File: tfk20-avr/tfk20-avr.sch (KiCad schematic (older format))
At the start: 31 parts, among them J1 USB_C_Receptacle_USB2.0, J2 AVR-ISP-6, SW1 Reset, U1 ATmega32U4-AU, Y1 16MHz

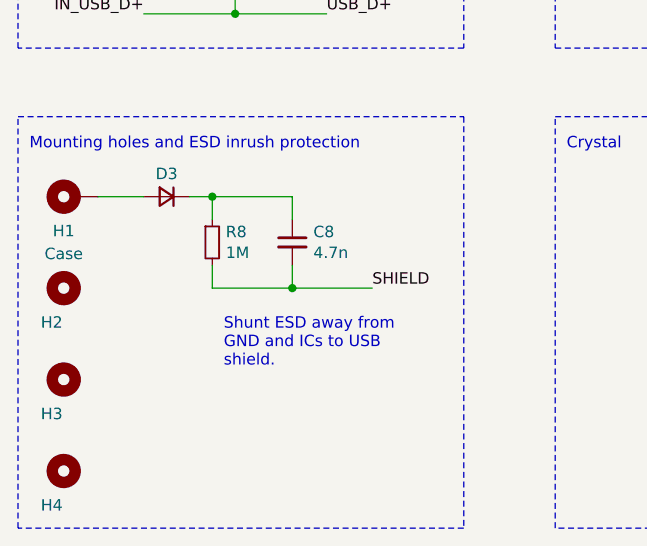
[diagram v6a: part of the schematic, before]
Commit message: Finish north-facing LED footprint layout
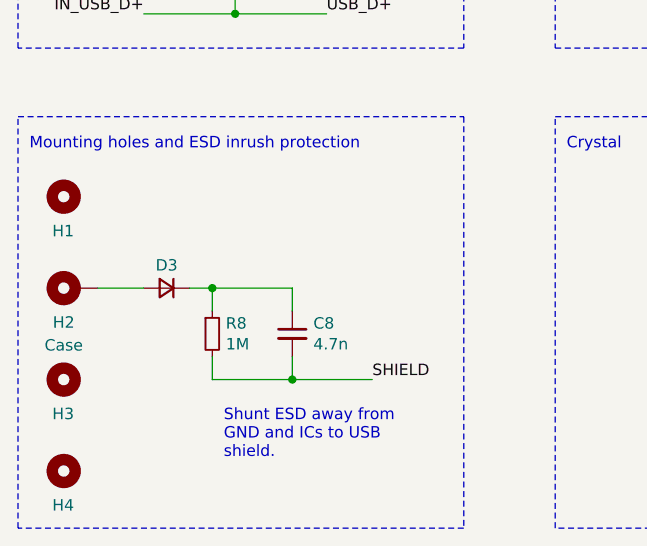
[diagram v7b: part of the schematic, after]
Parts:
- renumbered H2 to H1, H1 to H2
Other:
- moved on the sheet: C8, D3, H1, H2, R8
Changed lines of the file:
@@
 L Device:D_Small D3
 U 1 1 60989164
-P 1350 6150
+P 1350 6550
 AR Path="/60989164" Ref="D3"  Part="1"
 AR Path="/60815FFC/60989164" Ref="D?"  Part="1"
-F 0 "D3" H 1350 6050 50  0000 C CNN
-F 1 "Case ESD" H 1350 6034 50  0001 C CNN
-F 2 "Diode_SMD:D_SOD-123" V 1350 6150 50  0001 C CNN
-F 3 "~" V 1350 6150 50  0001 C CNN
-	1    1350 6150
+F 0 "D3" H 1350 6450 50  0000 C CNN
+F 1 "Case ESD" H 1350 6434 50  0001 C CNN
+F 2 "Diode_SMD:D_SOD-123" V 1350 6550 50  0001 C CNN
+F 3 "~" V 1350 6550 50  0001 C CNN
+	1    1350 6550
 	-1   0    0    1
 $EndComp
 Wire Wire Line
-	1450 6150 1550 6150
-Wire Wire Line
-	1550 6150 1550 6250
-Wire Wire Line
-	1550 6150 1900 6150
-Wire Wire Line
-	1900 6150 1900 6250
-Connection ~ 1550 6150
+	1450 6550 1550 6550
+Wire Wire Line
+	1550 6550 1550 6650
+Wire Wire Line
+	1550 6550 1900 6550
+Wire Wire Line
+	1900 6550 1900 6650
+Connection ~ 1550 6550
 $Comp
 L Device:R_Small R8
 U 1 1 6098916F
-P 1550 6350
+P 1550 6750
 AR Path="/6098916F" Ref="R8"  Part="1"
 AR Path="/60815FFC/6098916F" Ref="R?"  Part="1"
-F 0 "R8" H 1609 6396 50  0000 L CNN
-F 1 "1M" H 1609 6305 50  0000 L CNN
-F 2 "Resistor_SMD:R_0805_2012Metric_Pad1.20x1.40mm_HandSolder" H 1550 6350 50  0001 C CNN
-F 3 "~" H 1550 6350 50  0001 C CNN
-	1    1550 6350
+F 0 "R8" H 1609 6796 50  0000 L CNN
+F 1 "1M" H 1609 6705 50  0000 L CNN
+F 2 "Resistor_SMD:R_0805_2012Metric_Pad1.20x1.40mm_HandSolder" H 1550 6750 50  0001 C CNN
+F 3 "~" H 1550 6750 50  0001 C CNN
+	1    1550 6750
 	1    0    0    -1
 $EndComp
@@
 L Device:C_Small C8
 U 1 1 60989175
-P 1900 6350
+P 1900 6750
 AR Path="/60989175" Ref="C8"  Part="1"
 AR Path="/60815FFC/60989175" Ref="C?"  Part="1"
-F 0 "C8" H 1992 6396 50  0000 L CNN
-F 1 "4.7n" H 1992 6305 50  0000 L CNN
-F 2 "Capacitor_SMD:C_0805_2012Metric_Pad1.18x1.45mm_HandSolder" H 1900 6350 50  0001 C CNN
-F 3 "~" H 1900 6350 50  0001 C CNN
-	1    1900 6350
-	1    0    0    -1
-$EndComp
-Wire Wire Line
-	1900 6450 1900 6550
-Wire Wire Line
-	1900 6550 1550 6550
-Wire Wire Line
-	1550 6550 1550 6450
+F 0 "C8" H 1992 6796 50  0000 L CNN
+F 1 "4.7n" H 1992 6705 50  0000 L CNN
+F 2 "Capacitor_SMD:C_0805_2012Metric_Pad1.18x1.45mm_HandSolder" H 1900 6750 50  0001 C CNN
+F 3 "~" H 1900 6750 50  0001 C CNN
+	1    1900 6750
+	1    0    0    -1
+$EndComp
+Wire Wire Line
+	1900 6850 1900 6950
+Wire Wire Line
+	1900 6950 1550 6950
+Wire Wire Line
+	1550 6950 1550 6850
 Text Notes 750  5950 0    50   ~ 0
 Mounting holes and ESD inrush protection
@@
 	700  7600 700  5800
 Wire Wire Line
-	1250 6150 1050 6150
-$Comp
-L Mechanical:MountingHole_Pad H1
+	1250 6550 1050 6550
+$Comp
+L Mechanical:MountingHole_Pad H2
 U 1 1 60989184
-P 950 6150
-AR Path="/60989184" Ref="H1"  Part="1"
+P 950 6550
+AR Path="/60989184" Ref="H2"  Part="1"
 AR Path="/60815FFC/60989184" Ref="H?"  Part="1"
-F 0 "H1" V 800 6200 50  0000 C CNN
-F 1 "Case" V 700 6200 50  0000 C CNN
-F 2 "MountingHole:MountingHole_2.5mm_Pad" H 950 6150 50  0001 C CNN
-F 3 "~" H 950 6150 50  0001 C CNN
-	1    950  6150
+F 0 "H2" V 800 6600 50  0000 C CNN
+F 1 "Case" V 700 6600 50  0000 C CNN
+F 2 "MountingHole:MountingHole_2.5mm_Pad" H 950 6550 50  0001 C CNN
+F 3 "~" H 950 6550 50  0001 C CNN
+	1    950  6550
 	0    -1   -1   0
 $EndComp
 Wire Wire Line
-	1900 6550 2250 6550
-Connection ~ 1900 6550
-Text Label 2250 6550 0    50   ~ 0
+	1900 6950 2250 6950
+Connection ~ 1900 6950
+Text Label 2250 6950 0    50   ~ 0
 SHIELD
-Text Notes 1600 6900 0    50   ~ 0
+Text Notes 1600 7300 0    50   ~ 0
 Shunt ESD away from \nGND and ICs to USB \nshield.
 Wire Wire Line
@@
 	3600 1050 3850 1050
 $Comp
-L Mechanical:MountingHole H2
+L Mechanical:MountingHole H1
 U 1 1 60BC9C45
-P 900 6550
-F 0 "H2" H 800 6400 50  0000 L CNN
-F 1 "MountingHole" H 1000 6505 50  0001 L CNN
-F 2 "MountingHole:MountingHole_2.5mm_Pad" H 900 6550 50  0001 C CNN
-F 3 "~" H 900 6550 50  0001 C CNN
-	1    900  6550
+P 900 6150
+F 0 "H1" H 850 6000 50  0000 L CNN
+F 1 "MountingHole" H 800 5900 50  0001 L CNN
+F 2 "MountingHole:MountingHole_2.5mm_Pad" H 900 6150 50  0001 C CNN
+F 3 "~" H 900 6150 50  0001 C CNN
+	1    900  6150
 	1    0    0    -1
 $EndComp
@@
 U 1 1 60BCA1EE
 P 900 6950
-F 0 "H3" H 800 6800 50  0000 L CNN
+F 0 "H3" H 850 6800 50  0000 L CNN
 F 1 "MountingHole" H 1000 6905 50  0001 L CNN
 F 2 "MountingHole:MountingHole_2.5mm_Pad" H 900 6950 50  0001 C CNN
@@
 U 1 1 60BCA526
 P 900 7350
-F 0 "H4" H 800 7200 50  0000 L CNN
+F 0 "H4" H 850 7200 50  0000 L CNN
 F 1 "MountingHole" H 1000 7305 50  0001 L CNN
 F 2 "MountingHole:MountingHole_2.5mm_Pad" H 900 7350 50  0001 C CNN

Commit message: Continue routing
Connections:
- net GND: now also C10.2, C9.1, Y1.4
- net VBUS: now also D1.1 (K), F1.2, J1.A4 (VBUS), J1.A9 (VBUS), J1.B4 (VBUS), J1.B9 (VBUS)
- net MCU_USB_D-: now reaches R6.2, U1.3 (D-)
- net MCU_USB_D+: now reaches R5.2, U1.4 (D+)
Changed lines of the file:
@@
 	10050 3650 10150 3650
 Wire Wire Line
-	2800 1050 2800 1250
-Wire Wire Line
-	2800 1250 2400 1250
-$Comp
-L Device:D_Zener_Small D1
-U 1 1 60BED50D
-P 3600 1250
-F 0 "D1" V 3554 1320 50  0000 L CNN
-F 1 "5.5V" V 3645 1320 50  0000 L CNN
-F 2 "Diode_SMD:D_SOD-123" V 3600 1250 50  0001 C CNN
-F 3 "~" V 3600 1250 50  0001 C CNN
-	1    3600 1250
-	0    1    1    0
-$EndComp
-Wire Wire Line
-	3600 1350 3600 1450
-Connection ~ 3600 1450
-Wire Wire Line
-	2800 1050 3600 1050
-Wire Wire Line
-	3600 1150 3600 1050
-Connection ~ 3600 1050
-Wire Wire Line
-	3600 1050 3850 1050
+	3000 1050 3000 1250
+Wire Wire Line
+	3000 1250 2400 1250
 $Comp
 L Mechanical:MountingHole H1
@@
 Connection ~ 8800 1200
 Connection ~ 8800 1500
+$Comp
+L power:VBUS #PWR0101
+U 1 1 60C26DAA
+P 3000 1000
+F 0 "#PWR0101" H 3000 850 50  0001 C CNN
+F 1 "VBUS" H 3015 1173 50  0000 C CNN
+F 2 "" H 3000 1000 50  0001 C CNN
+F 3 "" H 3000 1000 50  0001 C CNN
+	1    3000 1000
+	1    0    0    -1
+$EndComp
+Wire Wire Line
+	3000 1000 3000 1050
+Connection ~ 3000 1050
+Text Label 8850 3750 2    39   ~ 0
+MCU_USB_D+
+Text Label 8850 3850 2    39   ~ 0
+MCU_USB_D-
+$Comp
+L power:GND #PWR0102
+U 1 1 60C2F48B
+P 5150 7350
+AR Path="/60C2F48B" Ref="#PWR0102"  Part="1"
+AR Path="/60815FFC/60C2F48B" Ref="#PWR?"  Part="1"
+F 0 "#PWR0102" H 5150 7100 50  0001 C CNN
+F 1 "GND" H 5155 7177 50  0000 C CNN
+F 2 "" H 5150 7350 50  0001 C CNN
+F 3 "" H 5150 7350 50  0001 C CNN
+	1    5150 7350
+	1    0    0    -1
+$EndComp
+Wire Wire Line
+	5150 7250 5150 7350
+Connection ~ 5150 7250
+Connection ~ 3600 1450
+Wire Wire Line
+	3000 1050 3600 1050
+Wire Wire Line
+	3600 1050 3850 1050
+Connection ~ 3600 1050
+Wire Wire Line
+	3600 1350 3600 1450
+Wire Wire Line
+	3600 1150 3600 1050
+$Comp
+L Device:D_Zener_Small D1
+U 1 1 60BED50D
+P 3600 1250
+F 0 "D1" V 3554 1320 50  0000 L CNN
+F 1 "5.5V" V 3645 1320 50  0000 L CNN
+F 2 "Diode_SMD:D_SOD-123" V 3600 1250 50  0001 C CNN
+F 3 "~" V 3600 1250 50  0001 C CNN
+	1    3600 1250
+	0    1    1    0
+$EndComp
 $EndSCHEMATC
